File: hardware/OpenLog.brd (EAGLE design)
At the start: 15.2 x 19.1 mm, 23 parts, among them Q1 16MHZ, U1 ATMEGA328P_TQFP, U2 3.3V MIC5205, U3 microSD Socket

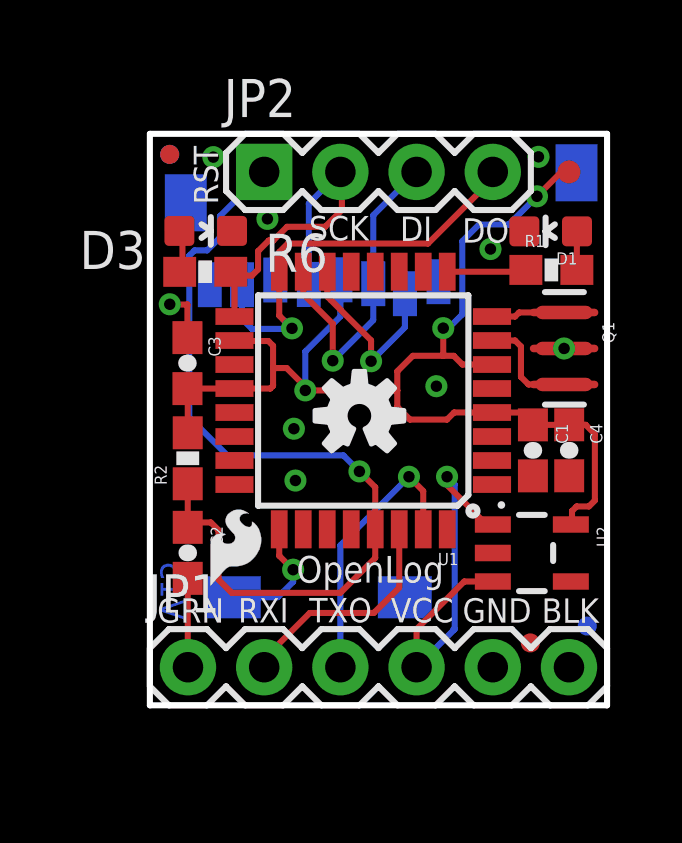
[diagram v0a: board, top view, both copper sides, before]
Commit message: Changed to 10uF tantalum. Added labels to bottom silk. Added TP vias.
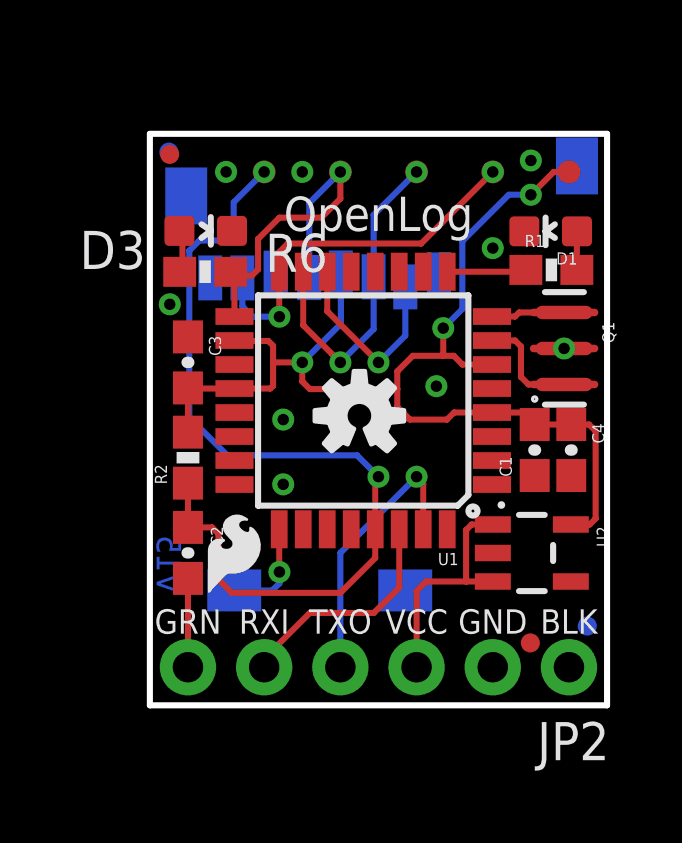
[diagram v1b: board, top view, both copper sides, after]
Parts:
- removed JP1: Serial Connection, SparkFun:1X06
- added TP2, TP3, TP4, TP5: TEST-POINT3, SparkFun-Passives:PAD.03X.03
- C1: value 1.0uF -> 10uF; device SparkFun-Capacitors:0603-CAP -> SparkFun-Capacitors:0603-POL
- FRAME1: value (none) -> FRAME-LETTER
- JP2: device SparkFun:1X04 -> SparkFun-Connectors:1X06_NO_SILK
- moved JP2 19.4 mm to (14.0, 1.27), turned to 180 degrees
- moved U3 0.23 mm to (14.7, 3.43)
- moved LOGO1 0.21 mm to (1.65, 3.43)
- moved FID4 0.08 mm to (0.64, 18.4)
- moved C4 0.07 mm to (14.0, 8.51)
- moved C1 0.06 mm to (12.8, 8.51), turned to 90 degrees
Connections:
- net 3.3V: now also C1.A; no longer C1.1
- net DTR: now also JP2.6; no longer JP1.1
- net GND: now also C1.K, JP2.1, JP2.2; no longer C1.2, JP1.5, JP1.6
- net MISO: now also TP2.P$1; no longer JP2.4
- net MOSI: now also TP3.P$1; no longer JP2.3
- net RAW: now also JP2.3; no longer JP1.4
- net RST: now also TP5.P$1; no longer JP2.1
- net RXI: now also JP2.5; no longer JP1.2
- net SCK: now also TP4.P$1; no longer JP2.2
- net TXO: now also JP2.4; no longer JP1.3
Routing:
- net RAW: track 13.8 -> 7.90 mm, vias 1 -> 0
- net MISO: track 14.7 -> 12.7 mm, vias 1 -> 2
- net GND: track 1.64 -> 0.00 mm
- net CD: track 4.13 -> 3.41 mm
- net 3.3V: track 40.2 -> 39.7 mm
- net MOSI: track 10.8 -> 11.3 mm, vias 1 -> 2
- net SCK: track 11.9 -> 11.6 mm, vias 0 -> 1
- net RST: track 29.2 -> 29.5 mm, vias 1 -> 2
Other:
- board text added: "+"
- board text added: "-"
- board text removed: "DI"
- board text removed: "DO"
- board text removed: "RST"
- board text removed: "SCK"

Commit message: Change to smaller OSHW logo. Moved top copper fiducials.
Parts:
- LOGO2: value OSHW-LOGOS -> OSHW-LOGOMINI; device SparkFun-Aesthetics:OSHW-LOGO-S -> SparkFun-Aesthetics:OSHW-LOGO-MINI
- moved FID1 13.9 mm to (14.6, 18.4)
- moved FID2 10.3 mm to (2.54, 0.51)
- moved LOGO2 9.44 mm to (1.78, 17.5)
- moved FID3 1.55 mm to (14.6, 4.19)
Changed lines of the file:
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@@
 <?xml version="1.0" encoding="utf-8"?>
 <!DOCTYPE eagle SYSTEM "eagle.dtd">
-<eagle version="7.1.0">
+<eagle version="7.2.0">
 <drawing>
 <settings>
@@
 <layer number="47" name="Measures" color="7" fill="1" visible="no" active="yes"/>
 <layer number="48" name="Document" color="7" fill="1" visible="no" active="yes"/>
-<layer number="49" name="Reference" color="7" fill="1" visible="yes" active="yes"/>
+<layer number="49" name="Reference" color="7" fill="1" visible="no" active="yes"/>
 <layer number="50" name="dxf" color="7" fill="1" visible="no" active="yes"/>
 <layer number="51" name="tDocu" color="6" fill="1" visible="yes" active="yes"/>
@@
 <element name="FRAME1" library="SparkFun-Aesthetics" package="CREATIVE_COMMONS" value="FRAME-LETTER" x="-21.062121875" y="-15.24"/>
 <element name="LOGO1" library="SparkFun-Aesthetics" package="SFE_LOGO_FLAME_.1" value="SFE_LOGO_FLAME.1_INCH" x="1.651" y="3.429"/>
-<element name="FID1" library="SparkFun-Aesthetics" package="MICRO-FIDUCIAL" value="FIDUCIALUFIDUCIAL" x="0.6604" y="18.3642"/>
-<element name="FID2" library="SparkFun-Aesthetics" package="MICRO-FIDUCIAL" value="FIDUCIALUFIDUCIAL" x="12.68221875" y="2.0802625"/>
+<element name="FID1" library="SparkFun-Aesthetics" package="MICRO-FIDUCIAL" value="FIDUCIALUFIDUCIAL" x="14.605" y="18.415"/>
+<element name="FID2" library="SparkFun-Aesthetics" package="MICRO-FIDUCIAL" value="FIDUCIALUFIDUCIAL" x="2.54" y="0.508"/>
 <element name="TP1" library="SparkFun-Passives" package="PAD.03X.03" value="TEST-POINT3" x="13.97" y="17.78"/>
-<element name="LOGO2" library="SparkFun-Aesthetics" package="OSHW-LOGO-S" value="OSHW-LOGOS" x="6.985" y="9.652"/>
-<element name="FID3" library="SparkFun-Aesthetics" package="MICRO-FIDUCIAL" value="FIDUCIALUFIDUCIAL" x="14.5796" y="2.6416" rot="MR0"/>
+<element name="LOGO2" library="SparkFun-Aesthetics" package="OSHW-LOGO-MINI" value="OSHW-LOGOMINI" x="1.778" y="17.526"/>
+<element name="FID3" library="SparkFun-Aesthetics" package="MICRO-FIDUCIAL" value="FIDUCIALUFIDUCIAL" x="14.605" y="4.191" rot="MR0"/>
 <element name="FID4" library="SparkFun-Aesthetics" package="MICRO-FIDUCIAL" value="FIDUCIALUFIDUCIAL" x="0.635" y="18.4404" rot="MR0"/>
 <element name="TP2" library="SparkFun-Passives" package="PAD.03X.03" value="TEST-POINT3" x="11.43" y="17.78" rot="R270"/>
@@
 <via x="5.08" y="17.78" extent="1-16" drill="0.381"/>
 <via x="12.7" y="18.161" extent="1-16" drill="0.381"/>
-<via x="2.54" y="17.78" extent="1-16" drill="0.381"/>
+<via x="1.778" y="17.526" extent="1-16" drill="0.381"/>
 <via x="4.445" y="7.366" extent="1-16" drill="0.381"/>
 <via x="11.43" y="15.24" extent="1-16" drill="0.381"/>
